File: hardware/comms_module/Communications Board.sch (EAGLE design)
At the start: 103 parts, among them U1 Value, U2 STC3115, U3 TCA9554A_PW_16, X2 USB-MICROB, Y1 32.768kHz, Y2 24MHz

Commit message: Add extra cap footprint for the 1V3 regulator.
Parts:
- added C27: DNP, SparkFun-Passives:CAP0402-CAP
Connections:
- net GND: now also C27.2
- net PERIPHERAL_VCC: now also C27.1
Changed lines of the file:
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@@
 <part name="R30" library="SparkFun-Passives" deviceset="RESISTOR" device="0402-RES" value="1Meg"/>
 <part name="GND52" library="supply1" deviceset="GND" device=""/>
+<part name="C27" library="SparkFun-Passives" deviceset="CAP" device="0402-CAP" value="DNP"/>
+<part name="GND53" library="SparkFun" deviceset="GND" device=""/>
 </parts>
 <sheets>
@@
 <wire x1="231.14" y1="63.5" x2="137.16" y2="63.5" width="0.1524" layer="97"/>
 <text x="139.7" y="86.36" size="1.778" layer="97">1V3 Regulator</text>
-<text x="139.7" y="66.04" size="1.778" layer="97">Place IN close to 3V3 reg.</text>
+<text x="187.96" y="86.36" size="1.778" layer="97">Place IN close to 3V3 reg.</text>
 <wire x1="137.16" y1="93.98" x2="137.16" y2="127" width="0.1524" layer="97"/>
 <wire x1="137.16" y1="127" x2="231.14" y2="127" width="0.1524" layer="97"/>
@@
 <instance part="R30" gate="G$1" x="439.42" y="73.66" rot="R90"/>
 <instance part="GND52" gate="1" x="439.42" y="66.04"/>
+<instance part="C27" gate="G$1" x="152.4" y="73.66"/>
+<instance part="GND53" gate="1" x="152.4" y="68.58"/>
 </instances>
 <busses>
@@
 <pinref part="R30" gate="G$1" pin="1"/>
 <pinref part="GND52" gate="1" pin="GND"/>
+</segment>
+<segment>
+<pinref part="C27" gate="G$1" pin="2"/>
+<pinref part="GND53" gate="1" pin="GND"/>
 </segment>
 </net>
@@
 <wire x1="172.72" y1="71.12" x2="172.72" y2="78.74" width="0.1524" layer="91"/>
 <junction x="172.72" y="78.74"/>
-</segment>
-</net>
+<pinref part="C27" gate="G$1" pin="1"/>
+</segment>
+</net>

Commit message: Fixes from PCB review session.
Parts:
- removed R13: 1Meg, SparkFun-Passives:RESISTOR0603-RES
- removed R16, R18: 100Meg, SparkFun-Passives:RESISTOR0603-RES
- removed R19: 10k, SparkFun-Passives:RESISTOR0603-RES
- removed U$6, U$7: DMC2990UDJ, Capstone Library:DMC2990UDJ
- added SJ1: (no value), jumper:SJ2W
- R17: value 1M -> DNM
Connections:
- removed net N$12: R13.1, U$6G$2.D
- removed net N$21: R16.2, U$7G$1.D
- removed net N$22: R18.2, R19.2, U$6G$2.S, U$7G$1.G, U$7G$2.G
- removed net N$9: R13.2, U$6G$1.D, U$6G$1.G
- new net N$26: SJ1.2, U2.VCC
- net +3V3: now also SJ1.1; no longer R11.2, R12.2, R19.1, U2.VCC
- net /SYSDISBL_PF: no longer U$6G$2.G
- net BAT+: no longer R18.1, U$7G$2.S
- net GND: no longer U$6G$1.S, U$7G$1.S
- net PERIPHERAL_VCC: now also R11.2, R12.2, SJ1.3
- net SYSOFF: no longer R16.1, U$7G$2.D

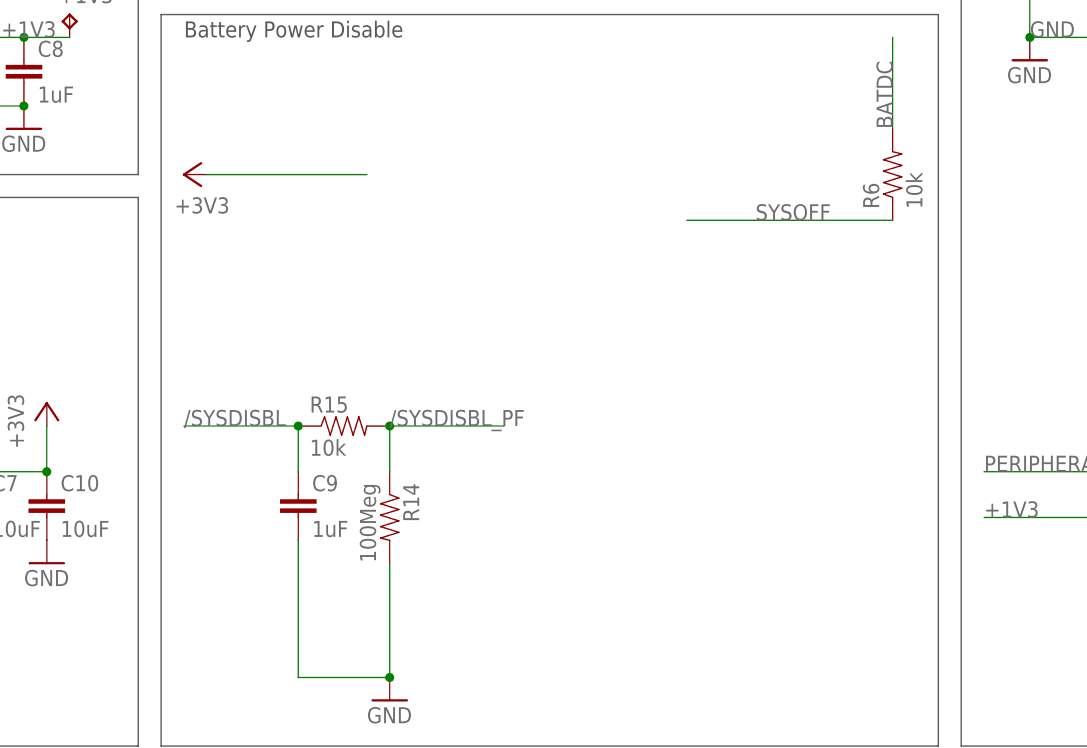
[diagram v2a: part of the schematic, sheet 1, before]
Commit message: Replace poweroff circuit with NOR gate.
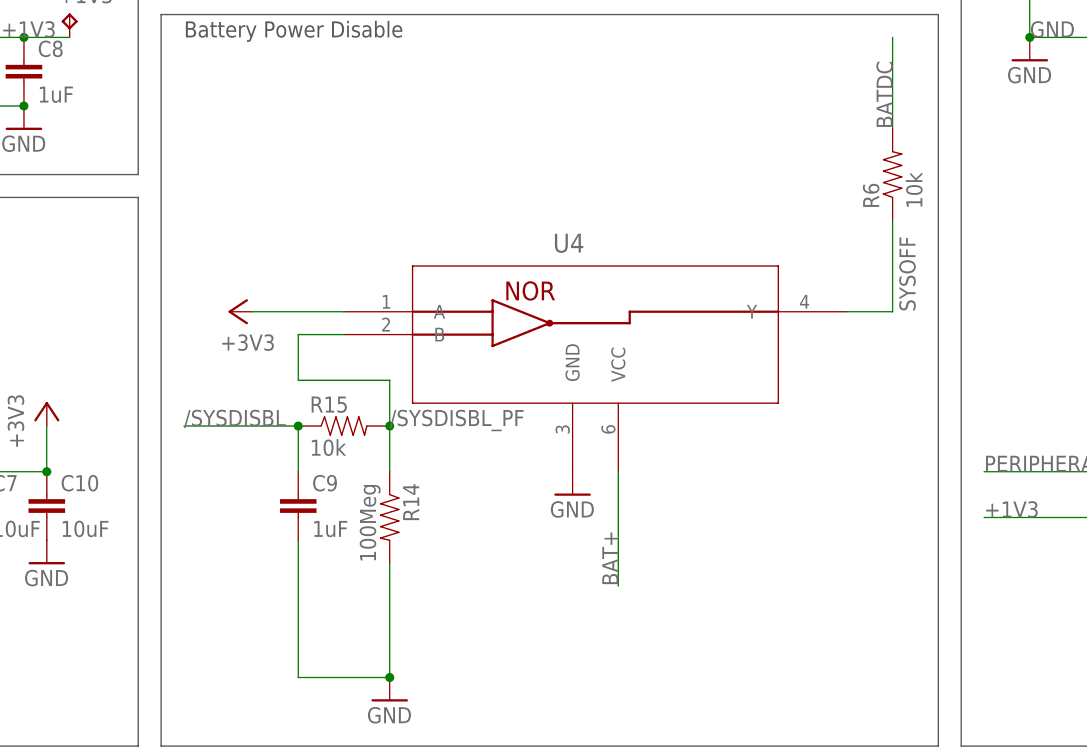
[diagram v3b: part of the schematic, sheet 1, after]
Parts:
- added U4: SN74AUP1G02_DSF_6, Capstone Library:SN74AUP1G02_DSF_6
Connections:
- net +3V3: now also U4.A
- net /SYSDISBL_PF: now also U4.B
- net BAT+: now also U4.VCC
- net GND: now also U4.GND
- net SYSOFF: now also U4.Y
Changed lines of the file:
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@@
 <part name="+3V5" library="supply1" deviceset="+3V3" device=""/>
 <part name="R10" library="SparkFun-Passives" deviceset="RESISTOR" device="0603-RES" value="500"/>
+<part name="U4" library="Capstone Library" deviceset="SN74AUP1G02_DSF_6" device=""/>
+<part name="GND54" library="SparkFun" deviceset="GND" device=""/>
 </parts>
 <sheets>
@@
 <instance part="GND18" gate="1" x="259.08" y="5.08"/>
 <instance part="R6" gate="G$1" x="314.96" y="63.5" rot="R90"/>
-<instance part="+3V4" gate="G$1" x="236.22" y="63.5" rot="R90"/>
+<instance part="+3V4" gate="G$1" x="241.3" y="48.26" rot="R90"/>
 <instance part="C10" gate="G$1" x="220.98" y="25.4"/>
 <instance part="GND21" gate="1" x="220.98" y="20.32"/>
@@
 <instance part="+3V5" gate="G$1" x="83.82" y="55.88"/>
 <instance part="R10" gate="G$1" x="281.94" y="93.98"/>
+<instance part="U4" gate="A" x="254" y="48.26"/>
+<instance part="GND54" gate="1" x="279.4" y="27.94"/>
 </instances>
 <busses>
@@
 <pinref part="R10" gate="G$1" pin="2"/>
 </segment>
+<segment>
+<pinref part="U4" gate="A" pin="GND"/>
+<pinref part="GND54" gate="1" pin="GND"/>
+</segment>
 </net>
 <net name="V_PREBUCK" class="0">
@@
 <wire x1="106.68" y1="7.62" x2="96.52" y2="7.62" width="0.1524" layer="91"/>
 <label x="96.52" y="7.62" size="1.778" layer="95"/>
+</segment>
+<segment>
+<pinref part="U4" gate="A" pin="VCC"/>
+<wire x1="284.48" y1="30.48" x2="284.48" y2="17.78" width="0.1524" layer="91"/>
+<label x="284.48" y="17.78" size="1.778" layer="95" rot="R90"/>
 </segment>
 </net>
@@
 </segment>
 <segment>
-<wire x1="256.54" y1="63.5" x2="238.76" y2="63.5" width="0.1524" layer="91"/>
+<wire x1="254" y1="48.26" x2="243.84" y2="48.26" width="0.1524" layer="91"/>
 <pinref part="+3V4" gate="G$1" pin="+3V3"/>
+<pinref part="U4" gate="A" pin="A"/>
 </segment>
 <segment>
@@
 <net name="SYSOFF" class="0">
 <segment>
-<wire x1="292.1" y1="58.42" x2="314.96" y2="58.42" width="0.1524" layer="91"/>
-<label x="299.72" y="58.42" size="1.778" layer="95"/>
+<wire x1="314.96" y1="48.26" x2="314.96" y2="58.42" width="0.1524" layer="91"/>
+<label x="317.5" y="48.26" size="1.778" layer="95" rot="R90"/>
 <pinref part="R6" gate="G$1" pin="1"/>
+<pinref part="U4" gate="A" pin="Y"/>
+<wire x1="314.96" y1="48.26" x2="309.88" y2="48.26" width="0.1524" layer="91"/>
 </segment>
 <segment>
@@
 <pinref part="R14" gate="G$1" pin="1"/>
 <wire x1="259.08" y1="35.56" x2="259.08" y2="30.48" width="0.1524" layer="91"/>
-<wire x1="271.78" y1="35.56" x2="259.08" y2="35.56" width="0.1524" layer="91"/>
+<label x="259.08" y="35.56" size="1.778" layer="95"/>
+<wire x1="259.08" y1="35.56" x2="259.08" y2="40.64" width="0.1524" layer="91"/>
+<wire x1="259.08" y1="40.64" x2="248.92" y2="40.64" width="0.1524" layer="91"/>
+<wire x1="248.92" y1="40.64" x2="248.92" y2="45.72" width="0.1524" layer="91"/>
+<pinref part="U4" gate="A" pin="B"/>
+<wire x1="248.92" y1="45.72" x2="254" y2="45.72" width="0.1524" layer="91"/>
 <junction x="259.08" y="35.56"/>
-<label x="259.08" y="35.56" size="1.778" layer="95"/>
-</segment>
-</net>
+</segment>
+</net>

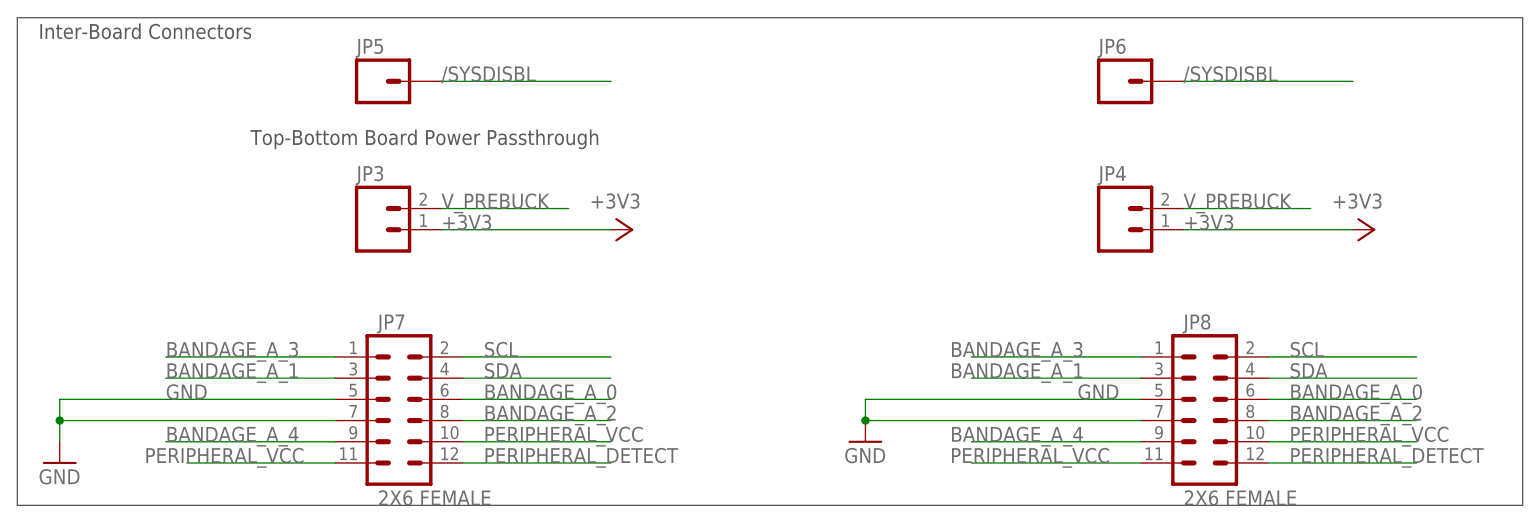
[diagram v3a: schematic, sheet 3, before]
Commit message: Finish routing of modified boards.
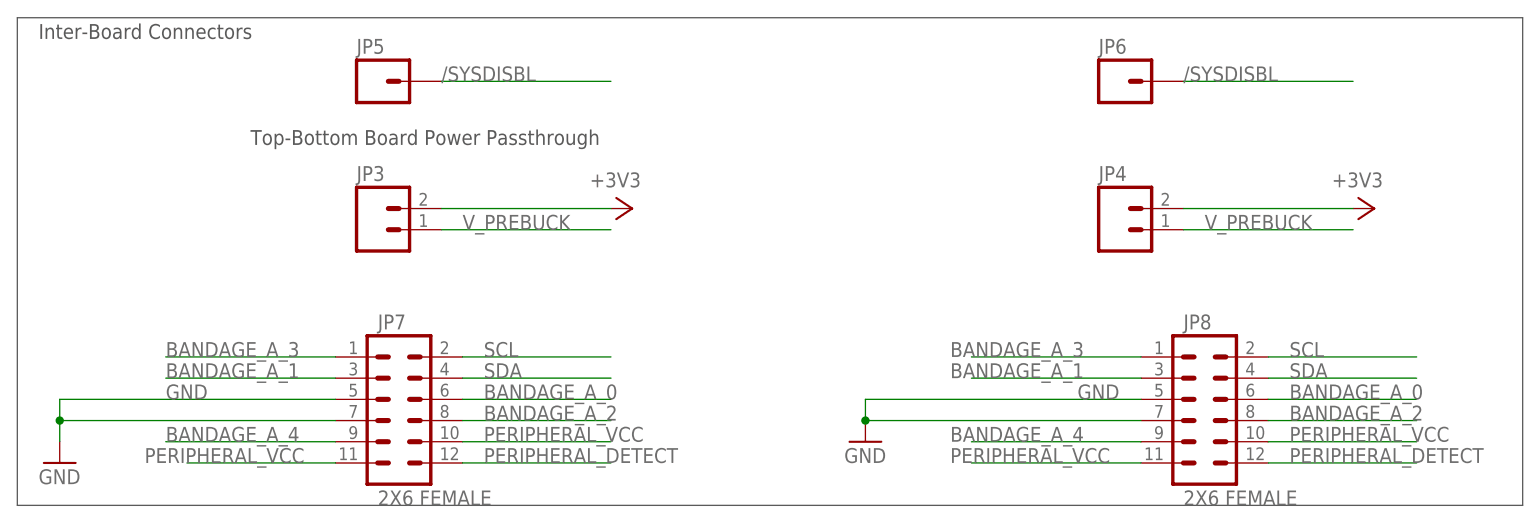
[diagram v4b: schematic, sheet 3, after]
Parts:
- X2: device SparkFun:USB-MICROB -> Capstone Library:USB-MICROB
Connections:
- net +3V3: now also JP3.2, JP4.2; no longer JP3.1, JP4.1
- net V_PREBUCK: now also JP3.1, JP4.1; no longer JP3.2, JP4.2
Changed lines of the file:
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@@
 <part name="GND21" library="SparkFun" deviceset="GND" device=""/>
 <part name="U$8" library="Capstone Library" deviceset="DMC2990UDJ" device=""/>
-<part name="X2" library="SparkFun" deviceset="USB" device="-MICROB"/>
+<part name="X2" library="Capstone Library" deviceset="USB" device="-MICROB"/>
 <part name="GND22" library="SparkFun" deviceset="GND" device=""/>
 <part name="B_EN" library="SparkFun-Connectors" deviceset="M02" device="PTH"/>
@@
 <instance part="GND20" gate="1" x="101.6" y="7.62"/>
 <instance part="JP3" gate="G$1" x="43.18" y="33.02"/>
-<instance part="+3V6" gate="G$1" x="73.66" y="33.02" rot="R270"/>
+<instance part="+3V6" gate="G$1" x="73.66" y="35.56" rot="R270"/>
 <instance part="JP4" gate="G$1" x="132.08" y="33.02"/>
-<instance part="+3V7" gate="G$1" x="162.56" y="33.02" rot="R270"/>
+<instance part="+3V7" gate="G$1" x="162.56" y="35.56" rot="R270"/>
 <instance part="JP5" gate="G$1" x="43.18" y="50.8"/>
 <instance part="JP6" gate="G$1" x="132.08" y="50.8"/>
@@
 </segment>
 </net>
-<net name="V_PREBUCK" class="0">
-<segment>
-<pinref part="JP3" gate="G$1" pin="2"/>
-<wire x1="50.8" y1="35.56" x2="66.04" y2="35.56" width="0.1524" layer="91"/>
-<label x="50.8" y="35.56" size="1.778" layer="95"/>
-</segment>
-<segment>
-<pinref part="JP4" gate="G$1" pin="2"/>
-<wire x1="139.7" y1="35.56" x2="154.94" y2="35.56" width="0.1524" layer="91"/>
-<label x="139.7" y="35.56" size="1.778" layer="95"/>
-</segment>
-</net>
 <net name="SDA" class="0">
 <segment>
@@
 </segment>
 </net>
-<net name="+3V3" class="0">
-<segment>
-<pinref part="JP3" gate="G$1" pin="1"/>
-<wire x1="50.8" y1="33.02" x2="71.12" y2="33.02" width="0.1524" layer="91"/>
-<pinref part="+3V6" gate="G$1" pin="+3V3"/>
-<label x="50.8" y="33.02" size="1.778" layer="95"/>
-</segment>
-<segment>
-<pinref part="JP4" gate="G$1" pin="1"/>
-<wire x1="139.7" y1="33.02" x2="160.02" y2="33.02" width="0.1524" layer="91"/>
-<pinref part="+3V7" gate="G$1" pin="+3V3"/>
-<label x="139.7" y="33.02" size="1.778" layer="95"/>
-</segment>
-</net>
 <net name="PERIPHERAL_VCC" class="0">
 <segment>
@@
 </segment>
 </net>
+<net name="+3V3" class="0">
+<segment>
+<pinref part="+3V6" gate="G$1" pin="+3V3"/>
+<pinref part="JP3" gate="G$1" pin="2"/>
+<wire x1="71.12" y1="35.56" x2="50.8" y2="35.56" width="0.1524" layer="91"/>
+</segment>
+<segment>
+<pinref part="JP4" gate="G$1" pin="2"/>
+<pinref part="+3V7" gate="G$1" pin="+3V3"/>
+<wire x1="139.7" y1="35.56" x2="160.02" y2="35.56" width="0.1524" layer="91"/>
+</segment>
+</net>
+<net name="V_PREBUCK" class="0">
+<segment>
+<pinref part="JP4" gate="G$1" pin="1"/>
+<wire x1="139.7" y1="33.02" x2="160.02" y2="33.02" width="0.1524" layer="91"/>
+<label x="142.24" y="33.02" size="1.778" layer="95"/>
+</segment>
+<segment>
+<pinref part="JP3" gate="G$1" pin="1"/>
+<wire x1="50.8" y1="33.02" x2="71.12" y2="33.02" width="0.1524" layer="91"/>
+<label x="53.34" y="33.02" size="1.778" layer="95"/>
+</segment>
+</net>
